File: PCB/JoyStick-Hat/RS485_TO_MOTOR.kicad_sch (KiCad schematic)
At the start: 2 parts, among them U4 MAX3535ECWI+T

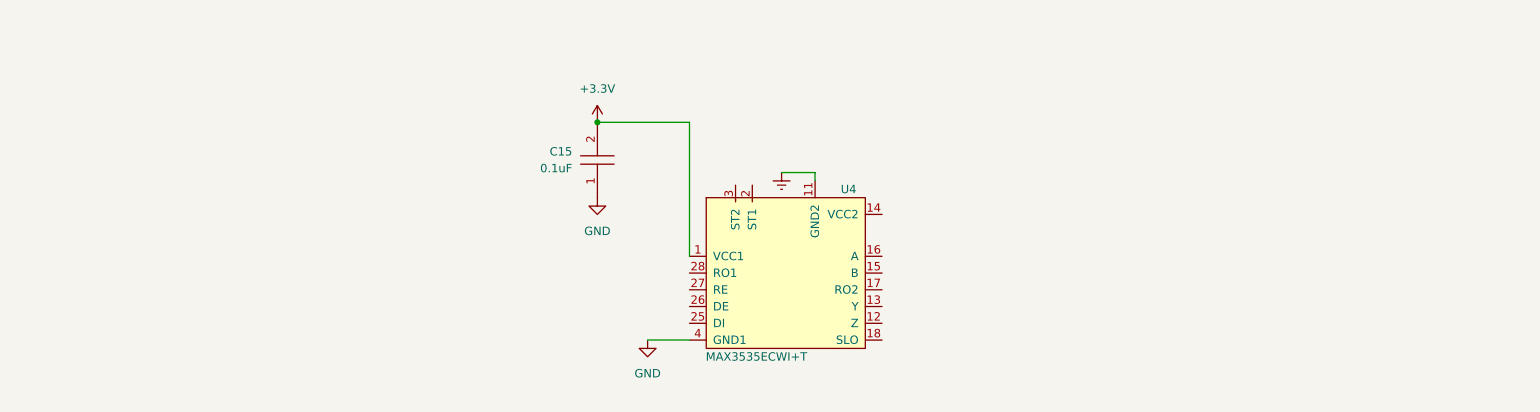
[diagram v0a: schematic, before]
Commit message: Schematic Progress
Made progress with schematic and corrected designator letters with connectors to match the built in paradigm of using J instead of T. T will not be used to referencing transformers instead of connectors.
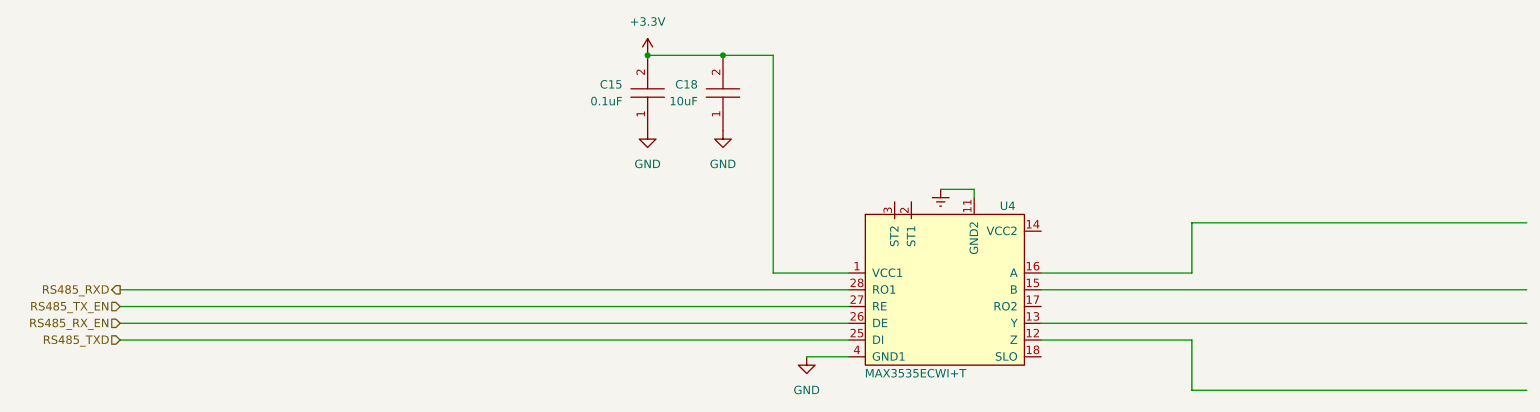
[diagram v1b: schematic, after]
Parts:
- added C18: CGA5L3X5R1V106K160AB, AVR-KiCAD-Lib-Capacitors:C1206, symbol AVR-KiCAD-Lib-Capacitors:CGA5L3X5R1V106K160AB
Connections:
- net +3.3V: now also C18.2
- net GND: now also C18.1
- net RS485_TXD: now reaches U4.25 (DI)
- net RS485_RX_EN: now reaches U4.26 (DE)
- net RS485_TX_EN: now reaches U4.27 (RE)
- net RS485_RXD: now reaches U4.28 (RO1)
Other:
- moved on the sheet: C15, U4

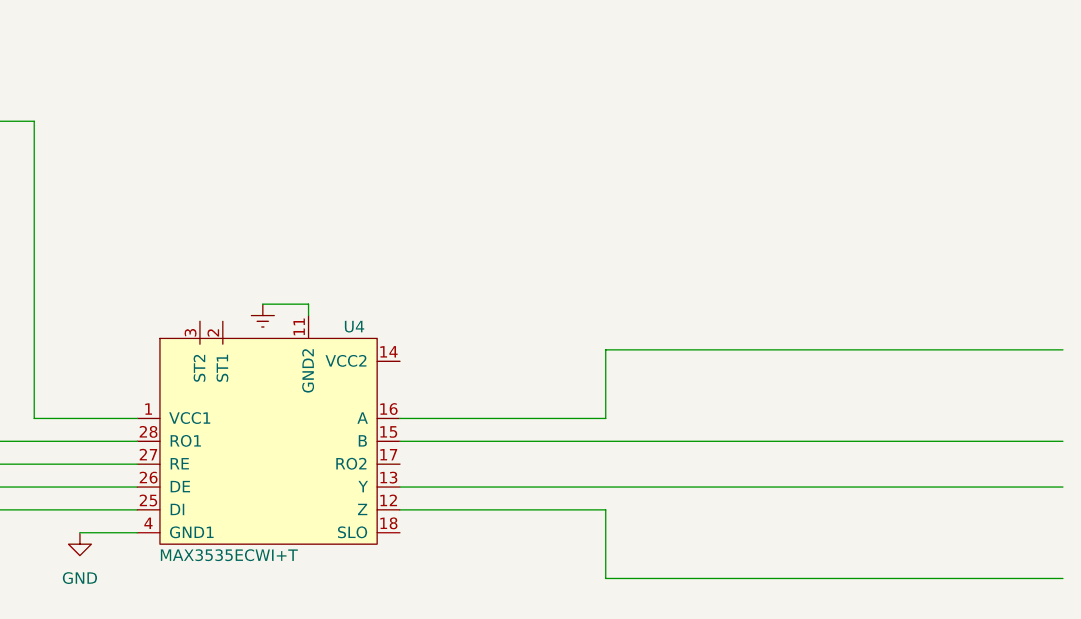
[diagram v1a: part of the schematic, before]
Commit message: Schematic Complete
Schematic completed. Moved to 100 pin version of STM32 MCU for more connectivity and better muxing of internal peripherals with pins.
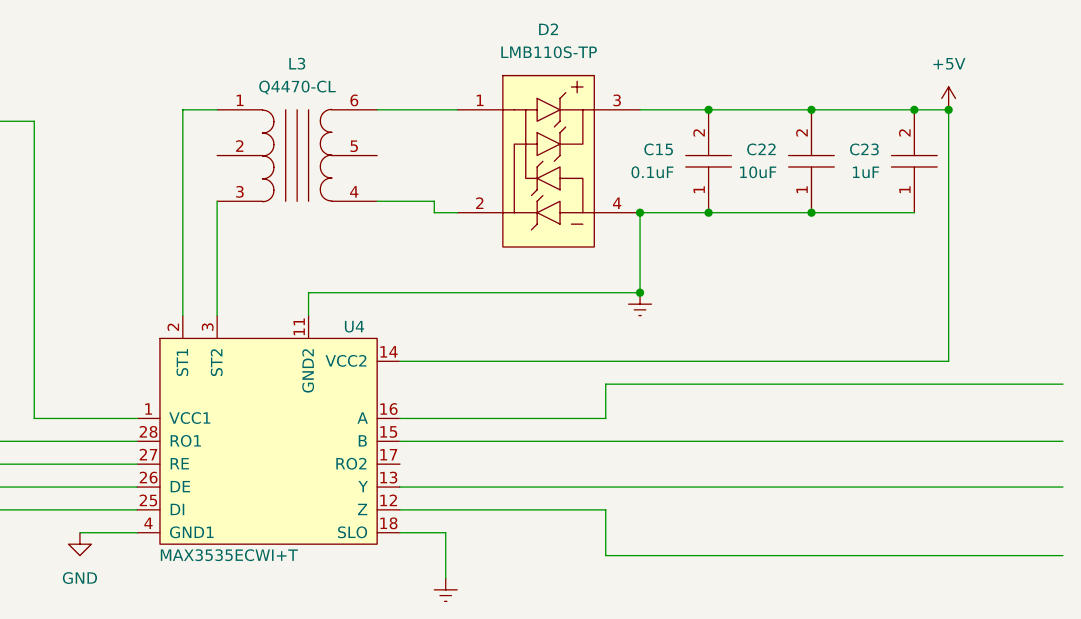
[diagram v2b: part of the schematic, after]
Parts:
- added C15: CL10B104JB8NNNC, AVR-KiCAD-Lib-Capacitors:C0603, symbol AVR-KiCAD-Lib-Capacitors:CL10B104JB8NNNC
- added C22: CGA5L3X5R1V106K160AB, AVR-KiCAD-Lib-Capacitors:C1206, symbol AVR-KiCAD-Lib-Capacitors:CGA5L3X5R1V106K160AB
- added C23: C1206C105K3RACAUTO, AVR-KiCAD-Lib-Diodes:D_SOD-123, symbol AVR-KiCAD-Lib-Capacitors:C1206C105K3RACAUTO
- added D2: LMB110S-TP, AVR-KiCAD-Lib-Diodes:LMB110S-TP, symbol AVR-KiCAD-Lib-Diodes:LMB110S-TP
- added L3: Q4470-CL, AVR-KiCAD-Lib-Transformers:SO6_Q4470-CL_C-SIZE_COC, symbol AVR-KiCAD-Lib-Transformers:Q4470-CL
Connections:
- net Earth: now also U4.18 (SLO), C15.1, C22.1, C23.1, D2.4
- net +5V: now reaches U4.14 (VCC2)
- net +5V: now also C15.2, C22.2, C23.2, D2.3
- net at U4.2 (ST1): now also L3.1
- net at U4.3 (ST2): now also L3.3
- new net: D2.1, L3.6
- new net: D2.2, L3.4

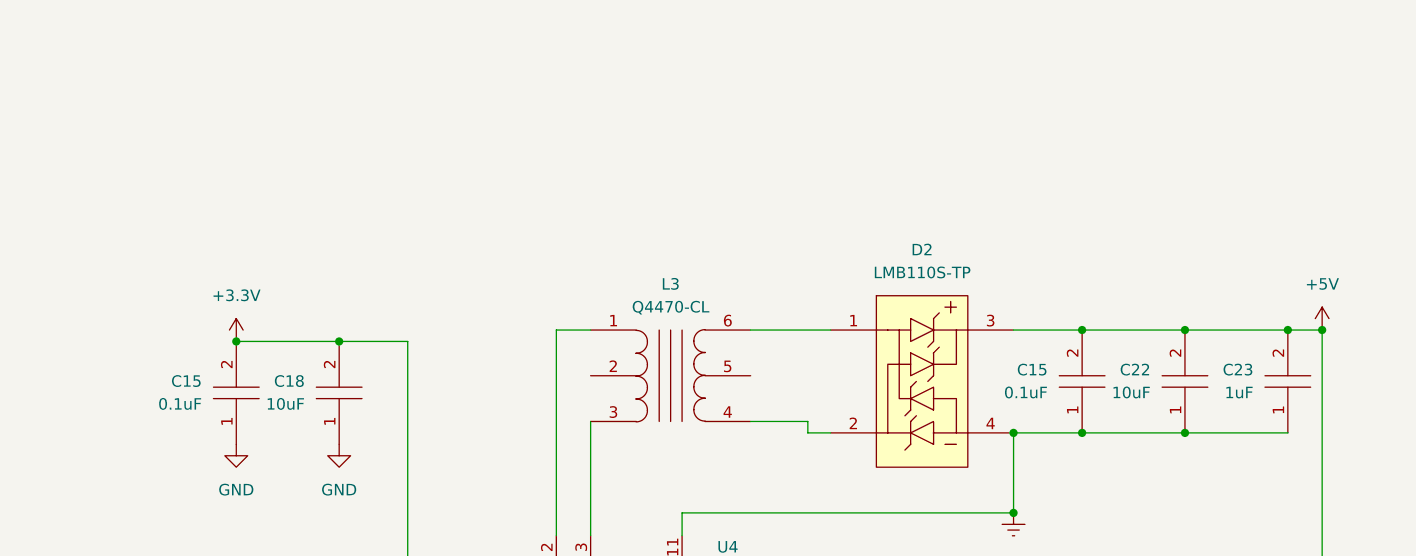
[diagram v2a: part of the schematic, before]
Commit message: LEDs and Additional connectors
Added heartbeat and diagnostic LEDs to STM32 and RPi3 schematics so we can directly flash them for debug purposes. Added a connector for serial port diagnostics on STM32. Added rotary switch interface for STM32 and added pullups to button connectors.
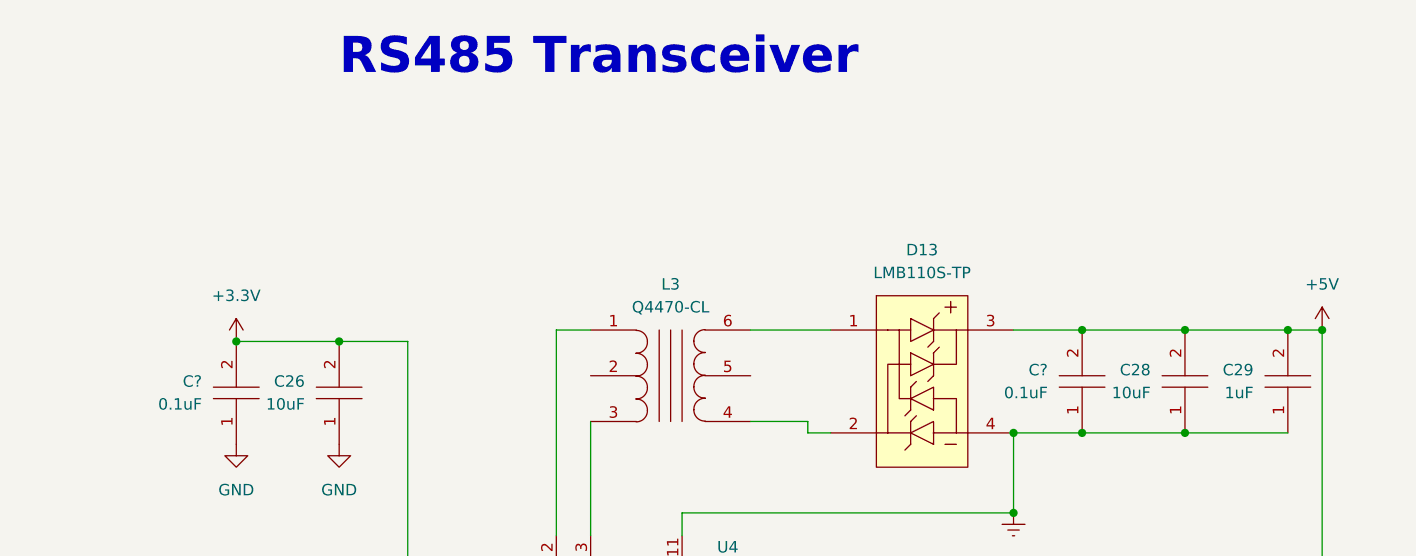
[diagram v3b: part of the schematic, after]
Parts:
- renumbered C18 to C26, C22 to C28, C23 to C29, C15 to C?, D2 to D13
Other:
- note added: "RS485 Transceiver"
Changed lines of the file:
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@@
     (stroke (width 0) (type default))
+  )
+  (text "RS485 Transceiver" (at 119.38 34.29 0)
+    (effects (font (size 4 4) (thickness 0.8) bold) (justify left bottom))
   )
   (hierarchical_label "RS485_TX_EN" (shape input) (at 27.94 101.6 180) (fields_autoplaced)
@@
   (symbol (lib_id "power:Earth") (at 172.72 114.3 0) (unit 1)
     (in_bom yes) (on_board yes) (dnp no) (fields_autoplaced)
-    (property "Reference" "#PWR08" (at 172.72 120.65 0)
+    (property "Reference" "#PWR068" (at 172.72 120.65 0)
       (effects (font (size 1.27 1.27)) hide)
     )
@@
       (project "JoyStick-Hat"
         (path "/cf0c81b5-5bdf-47c3-83c0-f6980f515e65/82e1f9af-1e5c-4e7f-8d36-34a266d2a8ff"
-          (reference "#PWR08") (unit 1)
+          (reference "#PWR068") (unit 1)
         )
       )
@@
   (symbol (lib_id "AVR-KiCAD-Lib-Capacitors:C1206C105K3RACAUTO") (at 224.79 68.58 90) (unit 1)
     (in_bom yes) (on_board yes) (dnp no) (fields_autoplaced)
-    (property "Reference" "C23" (at 220.98 66.675 90)
+    (property "Reference" "C29" (at 220.98 66.675 90)
       (effects (font (size 1.27 1.27)) (justify left))
     )
@@
       (project "JoyStick-Hat"
         (path "/cf0c81b5-5bdf-47c3-83c0-f6980f515e65/82e1f9af-1e5c-4e7f-8d36-34a266d2a8ff"
-          (reference "C23") (unit 1)
+          (reference "C29") (unit 1)
         )
       )
@@
   (symbol (lib_id "AVR-KiCAD-Lib-Capacitors:CGA5L3X5R1V106K160AB") (at 213.36 68.58 90) (unit 1)
     (in_bom yes) (on_board yes) (dnp no) (fields_autoplaced)
-    (property "Reference" "C22" (at 209.55 66.675 90)
+    (property "Reference" "C28" (at 209.55 66.675 90)
       (effects (font (size 1.27 1.27)) (justify left))
     )
@@
       (project "JoyStick-Hat"
         (path "/cf0c81b5-5bdf-47c3-83c0-f6980f515e65/82e1f9af-1e5c-4e7f-8d36-34a266d2a8ff"
-          (reference "C22") (unit 1)
+          (reference "C28") (unit 1)
         )
       )
@@
   (symbol (lib_id "power:GND") (at 107.95 74.93 0) (unit 1)
     (in_bom yes) (on_board yes) (dnp no) (fields_autoplaced)
-    (property "Reference" "#PWR044" (at 107.95 81.28 0)
+    (property "Reference" "#PWR065" (at 107.95 81.28 0)
       (effects (font (size 1.27 1.27)) hide)
     )
@@
       (project "JoyStick-Hat"
         (path "/cf0c81b5-5bdf-47c3-83c0-f6980f515e65/82e1f9af-1e5c-4e7f-8d36-34a266d2a8ff"
-          (reference "#PWR044") (unit 1)
+          (reference "#PWR065") (unit 1)
         )
       )
@@
   (symbol (lib_id "power:+5V") (at 228.6 62.23 0) (unit 1)
     (in_bom yes) (on_board yes) (dnp no) (fields_autoplaced)
-    (property "Reference" "#PWR051" (at 228.6 66.04 0)
+    (property "Reference" "#PWR070" (at 228.6 66.04 0)
       (effects (font (size 1.27 1.27)) hide)
     )
@@
       (project "JoyStick-Hat"
         (path "/cf0c81b5-5bdf-47c3-83c0-f6980f515e65/82e1f9af-1e5c-4e7f-8d36-34a266d2a8ff"
-          (reference "#PWR051") (unit 1)
+          (reference "#PWR070") (unit 1)
         )
       )
@@
   (symbol (lib_id "AVR-KiCAD-Lib-Capacitors:CL10B104JB8NNNC") (at 201.93 68.58 90) (unit 1)
     (in_bom yes) (on_board yes) (dnp no) (fields_autoplaced)
-    (property "Reference" "C15" (at 198.12 66.675 90)
+    (property "Reference" "C?" (at 198.12 66.675 90)
       (effects (font (size 1.27 1.27)) (justify left))
     )
@@
       (project "JoyStick-Hat"
         (path "/cf0c81b5-5bdf-47c3-83c0-f6980f515e65/be3abc89-1576-4d8d-a97c-6d68900a596b"
-          (reference "C15") (unit 1)
-        )
-        (path "/cf0c81b5-5bdf-47c3-83c0-f6980f515e65/82e1f9af-1e5c-4e7f-8d36-34a266d2a8ff"
-          (reference "C21") (unit 1)
+          (reference "C?") (unit 1)
+        )
+        (path "/cf0c81b5-5bdf-47c3-83c0-f6980f515e65/82e1f9af-1e5c-4e7f-8d36-34a266d2a8ff"
+          (reference "C27") (unit 1)
         )
       )
@@
   (symbol (lib_id "AVR-KiCAD-Lib-Capacitors:CL10B104JB8NNNC") (at 107.95 69.85 90) (unit 1)
     (in_bom yes) (on_board yes) (dnp no) (fields_autoplaced)
-    (property "Reference" "C15" (at 104.14 67.945 90)
+    (property "Reference" "C?" (at 104.14 67.945 90)
       (effects (font (size 1.27 1.27)) (justify left))
     )
@@
       (project "JoyStick-Hat"
         (path "/cf0c81b5-5bdf-47c3-83c0-f6980f515e65/be3abc89-1576-4d8d-a97c-6d68900a596b"
-          (reference "C15") (unit 1)
-        )
-        (path "/cf0c81b5-5bdf-47c3-83c0-f6980f515e65/82e1f9af-1e5c-4e7f-8d36-34a266d2a8ff"
-          (reference "C17") (unit 1)
+          (reference "C?") (unit 1)
+        )
+        (path "/cf0c81b5-5bdf-47c3-83c0-f6980f515e65/82e1f9af-1e5c-4e7f-8d36-34a266d2a8ff"
+          (reference "C25") (unit 1)
         )
       )
@@
   (symbol (lib_id "AVR-KiCAD-Lib-Capacitors:CGA5L3X5R1V106K160AB") (at 119.38 69.85 90) (unit 1)
     (in_bom yes) (on_board yes) (dnp no) (fields_autoplaced)
-    (property "Reference" "C18" (at 115.57 67.945 90)
+    (property "Reference" "C26" (at 115.57 67.945 90)
       (effects (font (size 1.27 1.27)) (justify left))
     )
@@
       (project "JoyStick-Hat"
         (path "/cf0c81b5-5bdf-47c3-83c0-f6980f515e65/82e1f9af-1e5c-4e7f-8d36-34a266d2a8ff"
-          (reference "C18") (unit 1)
+          (reference "C26") (unit 1)
         )
       )
@@
   (symbol (lib_id "power:GND") (at 119.38 74.93 0) (unit 1)
     (in_bom yes) (on_board yes) (dnp no) (fields_autoplaced)
-    (property "Reference" "#PWR047" (at 119.38 81.28 0)
+    (property "Reference" "#PWR066" (at 119.38 81.28 0)
       (effects (font (size 1.27 1.27)) hide)
     )
@@
       (project "JoyStick-Hat"
         (path "/cf0c81b5-5bdf-47c3-83c0-f6980f515e65/82e1f9af-1e5c-4e7f-8d36-34a266d2a8ff"
-          (reference "#PWR047") (unit 1)
+          (reference "#PWR066") (unit 1)
         )
       )
@@
   (symbol (lib_id "power:GND") (at 132.08 109.22 0) (unit 1)
     (in_bom yes) (on_board yes) (dnp no) (fields_autoplaced)
-    (property "Reference" "#PWR045" (at 132.08 115.57 0)
+    (property "Reference" "#PWR067" (at 132.08 115.57 0)
       (effects (font (size 1.27 1.27)) hide)
     )
@@
       (project "JoyStick-Hat"
         (path "/cf0c81b5-5bdf-47c3-83c0-f6980f515e65/82e1f9af-1e5c-4e7f-8d36-34a266d2a8ff"
-          (reference "#PWR045") (unit 1)
+          (reference "#PWR067") (unit 1)
         )
       )
@@
   (symbol (lib_id "power:+3.3V") (at 107.95 63.5 0) (unit 1)
     (in_bom yes) (on_board yes) (dnp no) (fields_autoplaced)
-    (property "Reference" "#PWR043" (at 107.95 67.31 0)
+    (property "Reference" "#PWR064" (at 107.95 67.31 0)
       (effects (font (size 1.27 1.27)) hide)
     )
@@
       (project "JoyStick-Hat"
         (path "/cf0c81b5-5bdf-47c3-83c0-f6980f515e65/82e1f9af-1e5c-4e7f-8d36-34a266d2a8ff"
-          (reference "#PWR043") (unit 1)
+          (reference "#PWR064") (unit 1)
         )
       )
@@
   (symbol (lib_id "AVR-KiCAD-Lib-Diodes:LMB110S-TP") (at 179.07 76.2 0) (unit 1)
     (in_bom yes) (on_board yes) (dnp no) (fields_autoplaced)
-    (property "Reference" "D2" (at 184.15 53.34 0)
+    (property "Reference" "D13" (at 184.15 53.34 0)
       (effects (font (size 1.27 1.27)))
     )
@@
       (project "JoyStick-Hat"
         (path "/cf0c81b5-5bdf-47c3-83c0-f6980f515e65/82e1f9af-1e5c-4e7f-8d36-34a266d2a8ff"
-          (reference "D2") (unit 1)
+          (reference "D13") (unit 1)
         )
       )
@@
   (symbol (lib_id "power:Earth") (at 194.31 82.55 0) (unit 1)
     (in_bom yes) (on_board yes) (dnp no) (fields_autoplaced)
-    (property "Reference" "#PWR046" (at 194.31 88.9 0)
+    (property "Reference" "#PWR069" (at 194.31 88.9 0)
       (effects (font (size 1.27 1.27)) hide)
     )
@@
       (project "JoyStick-Hat"
         (path "/cf0c81b5-5bdf-47c3-83c0-f6980f515e65/82e1f9af-1e5c-4e7f-8d36-34a266d2a8ff"
-          (reference "#PWR046") (unit 1)
-        )
-      )
+          (reference "#PWR069") (unit 1)
+        )
+      )

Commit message: Design Rules, Component Placement. Features Dropped
Added design rules for OSHPark.com to PCB, Most components placed roughly for whole board more to follow and more tweaks,. Features were dropped/rearanged. USB for STM32 dropped as its not necessary. LED driver and LEDs will be on separate board and SPI will run through cabling via differential transceiver that has yet to be added to schematic.
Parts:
- gave numbers to parts that had none: 2
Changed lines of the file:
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@@
     (instances
       (project "JoyStick-Hat"
-        (path "/cf0c81b5-5bdf-47c3-83c0-f6980f515e65/be3abc89-1576-4d8d-a97c-6d68900a596b"
-          (reference "C?") (unit 1)
-        )
         (path "/cf0c81b5-5bdf-47c3-83c0-f6980f515e65/82e1f9af-1e5c-4e7f-8d36-34a266d2a8ff"
           (reference "C27") (unit 1)
@@
     (instances
       (project "JoyStick-Hat"
-        (path "/cf0c81b5-5bdf-47c3-83c0-f6980f515e65/be3abc89-1576-4d8d-a97c-6d68900a596b"
-          (reference "C?") (unit 1)
-        )
         (path "/cf0c81b5-5bdf-47c3-83c0-f6980f515e65/82e1f9af-1e5c-4e7f-8d36-34a266d2a8ff"
           (reference "C25") (unit 1)
